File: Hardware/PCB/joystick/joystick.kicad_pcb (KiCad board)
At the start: 2 copper layers, 94 x 107 mm, 57 parts, among them J1 Synth_power_2x5, J11 AudioJack2, J12 3_pin_Molex_header, J13 AudioJack2, J14 2_pin_Molex_header, J4 AudioJack2, J5 6 pin Molex header, J6 AudioJack2, J7 3_pin_Molex_header, J8 2_pin_Molex_header, U1 TL074, U2 TL074

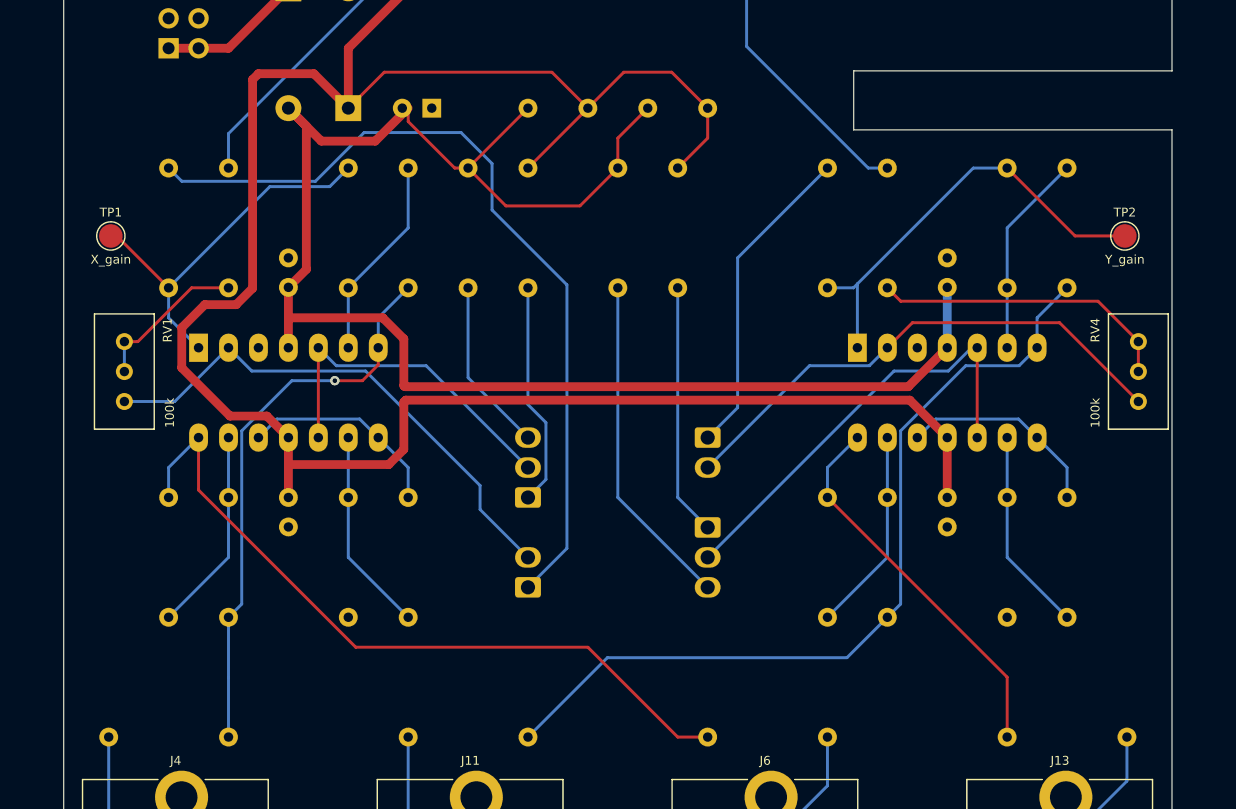
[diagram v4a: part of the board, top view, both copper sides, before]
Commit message: Change voltage ranges
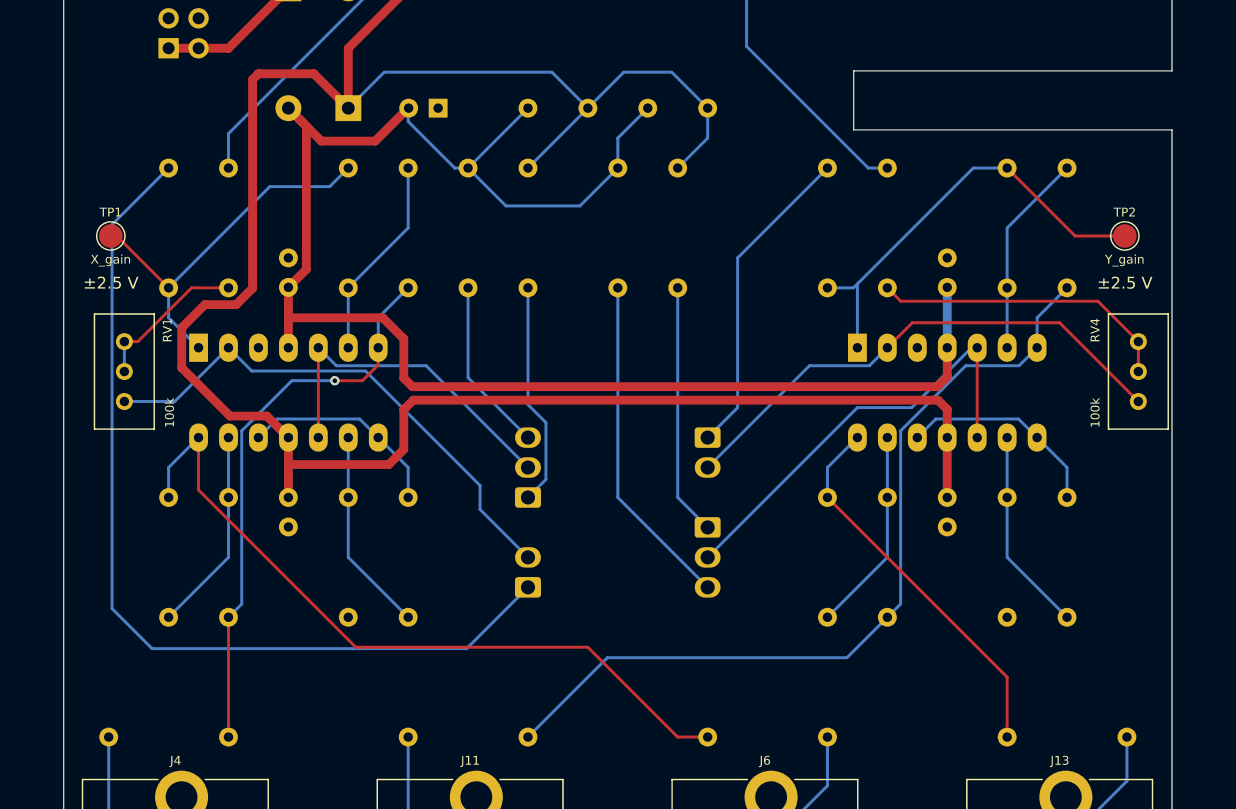
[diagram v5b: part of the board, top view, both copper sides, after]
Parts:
- R18, R19, R4, R5: value 330k -> 300k*
- moved C2 0.54 mm to (131.8, 80.2)
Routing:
- net XRANGEPOT_WIPER: track 70.6 -> 78.2 mm
- net -12V: track 137.7 -> 138.8 mm
- net +12V: track 182.6 -> 183.6 mm
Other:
- board text added: "* Adjust as needed, see build notes"
- board text added: "±2.5 V"

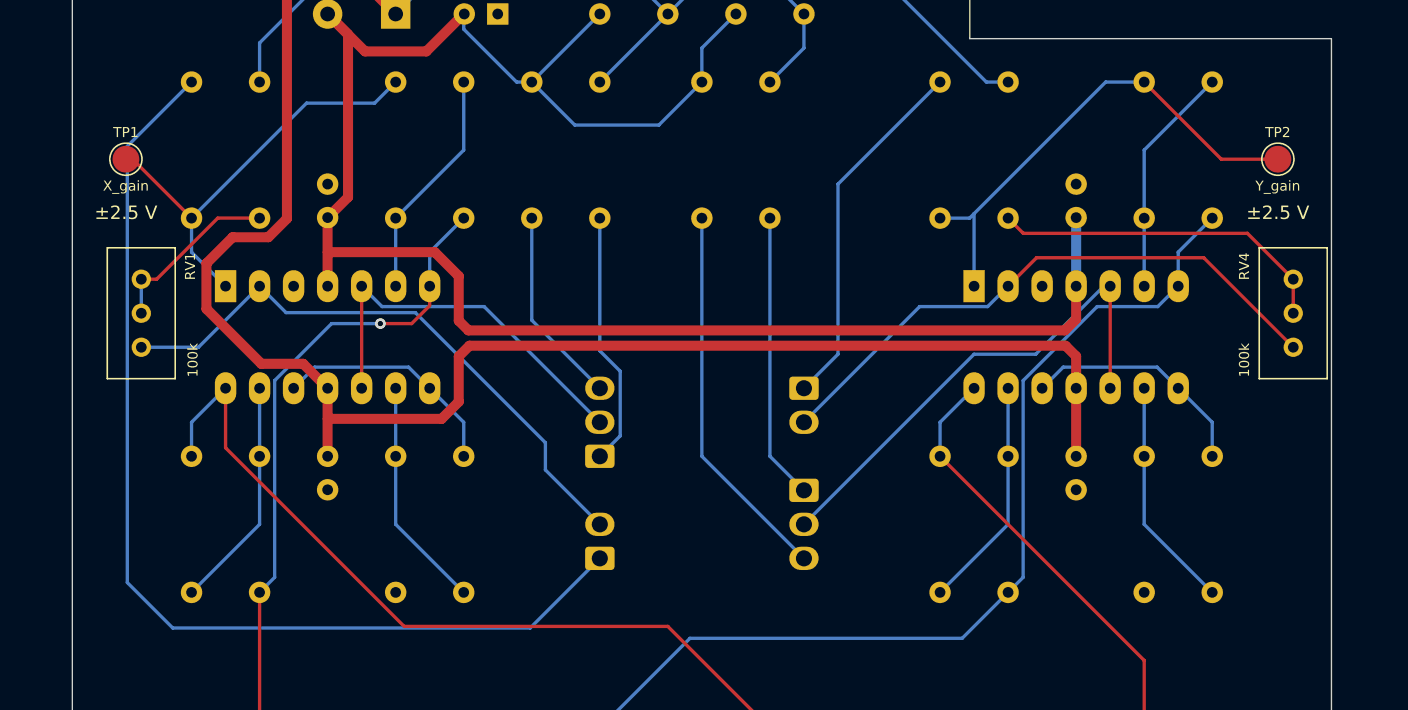
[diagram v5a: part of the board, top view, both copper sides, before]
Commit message: Move trimmers and TPs to back
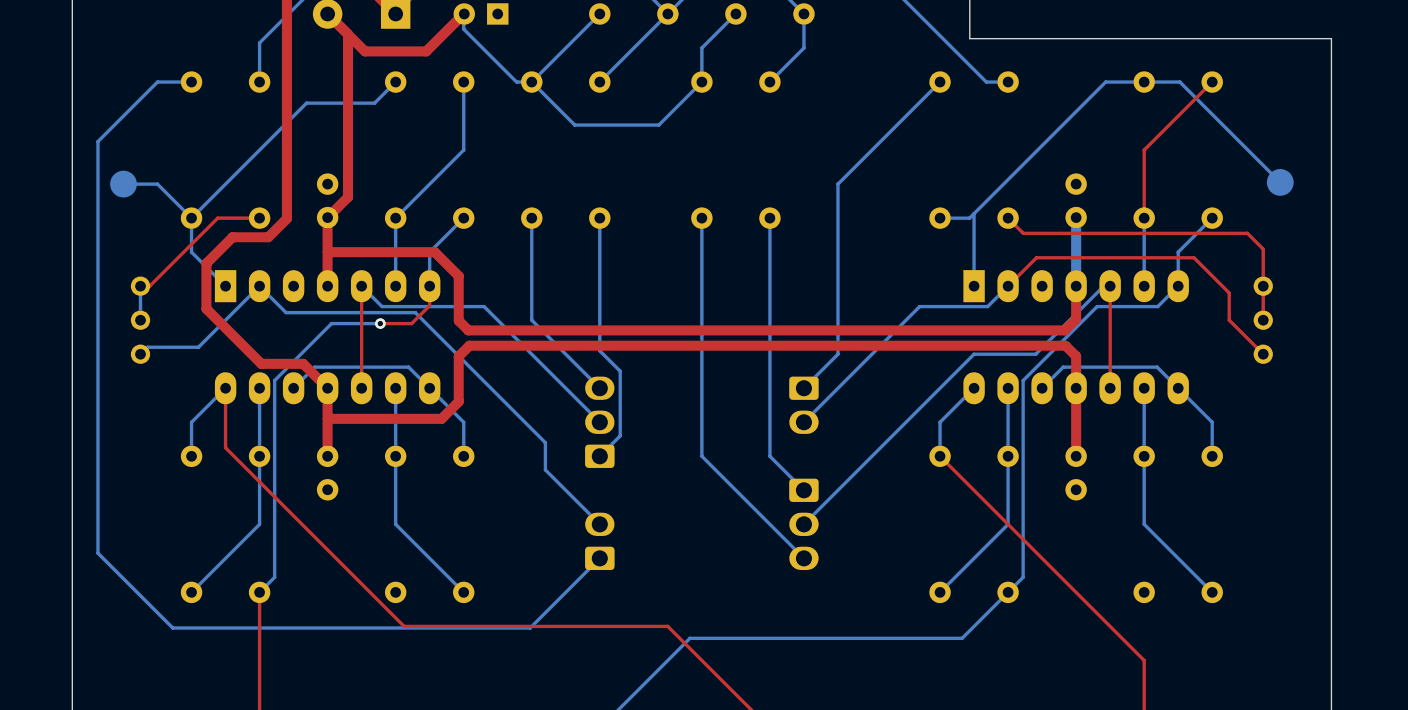
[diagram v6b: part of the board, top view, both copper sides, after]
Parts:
- RV1, RV4: footprint ao_tht:Potentiometer_Bourns_3296W_Vertical_screw_centered -> ao_tht:Potentiometer_Bourns_3296W_Vertical_standard; moved to B.Cu
- TP1, TP2: moved to B.Cu
- moved GRAF1 24.2 mm to (146.9, 70.0)
- moved TP1 1.87 mm to (103.8, 92.9)
- moved TP2 1.74 mm to (190.2, 92.7)
- moved RV1 1.18 mm to (105.1, 105.6)
- moved RV4 1.18 mm to (188.9, 105.6)
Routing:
- net XRANGEPOT_WIPER: track 78.2 -> 81.5 mm
- net Net-(R20-Pad1): track 37.2 -> 38.1 mm
- net YRANGEPOT_CCW: track 44.4 -> 43.6 mm
- net Net-(R6-Pad1): track 32.3 -> 31.7 mm

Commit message: Update docs, generate Gerbers
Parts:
- moved D1 11.4 mm to (124.1, 80.2), turned to 90 degrees
- moved D2 11.4 mm to (119.1, 70.0), turned to 270 degrees
- moved C4 2.54 mm to (119.1, 115.7), turned to 90 degrees
- moved C3 2.50 mm to (119.1, 95.4), turned to 90 degrees
- renumbered C2 to C1, C1 to C2, C4 to C3, C3 to C4, D2 to D1, D1 to D2
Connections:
- C1 pad 1: GND -> +12V
- C1 pad 2: -12V -> GND
- C2 pad 1: +12V -> GND
- C2 pad 2: GND -> -12V
- C3 pad 1: GND -> +12V
- C3 pad 2: -12V -> GND
- C4 pad 1: +12V -> GND
- C4 pad 2: GND -> -12V
- C5 pad 1: +12V -> -12V
- C6 pad 2: -12V -> +12V
- D1 pad 1: /-12_IN -> +12V
- D1 pad 2: -12V -> /+12_IN
- D2 pad 1: +12V -> /-12_IN
- D2 pad 2: /+12_IN -> -12V
- U1 pad 11: +12V -> -12V
- U1 pad 4: -12V -> +12V
- U2 pad 11: +12V -> -12V
- U2 pad 4: -12V -> +12V
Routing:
- net -12V: track 138.8 -> 175.3 mm
- net +12V: track 183.6 -> 147.8 mm

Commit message: Fix wrong R value; update documentation; images
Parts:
- R2: value 15k -> 20k
